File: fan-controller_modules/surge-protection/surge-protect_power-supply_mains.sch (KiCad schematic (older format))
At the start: 10 parts

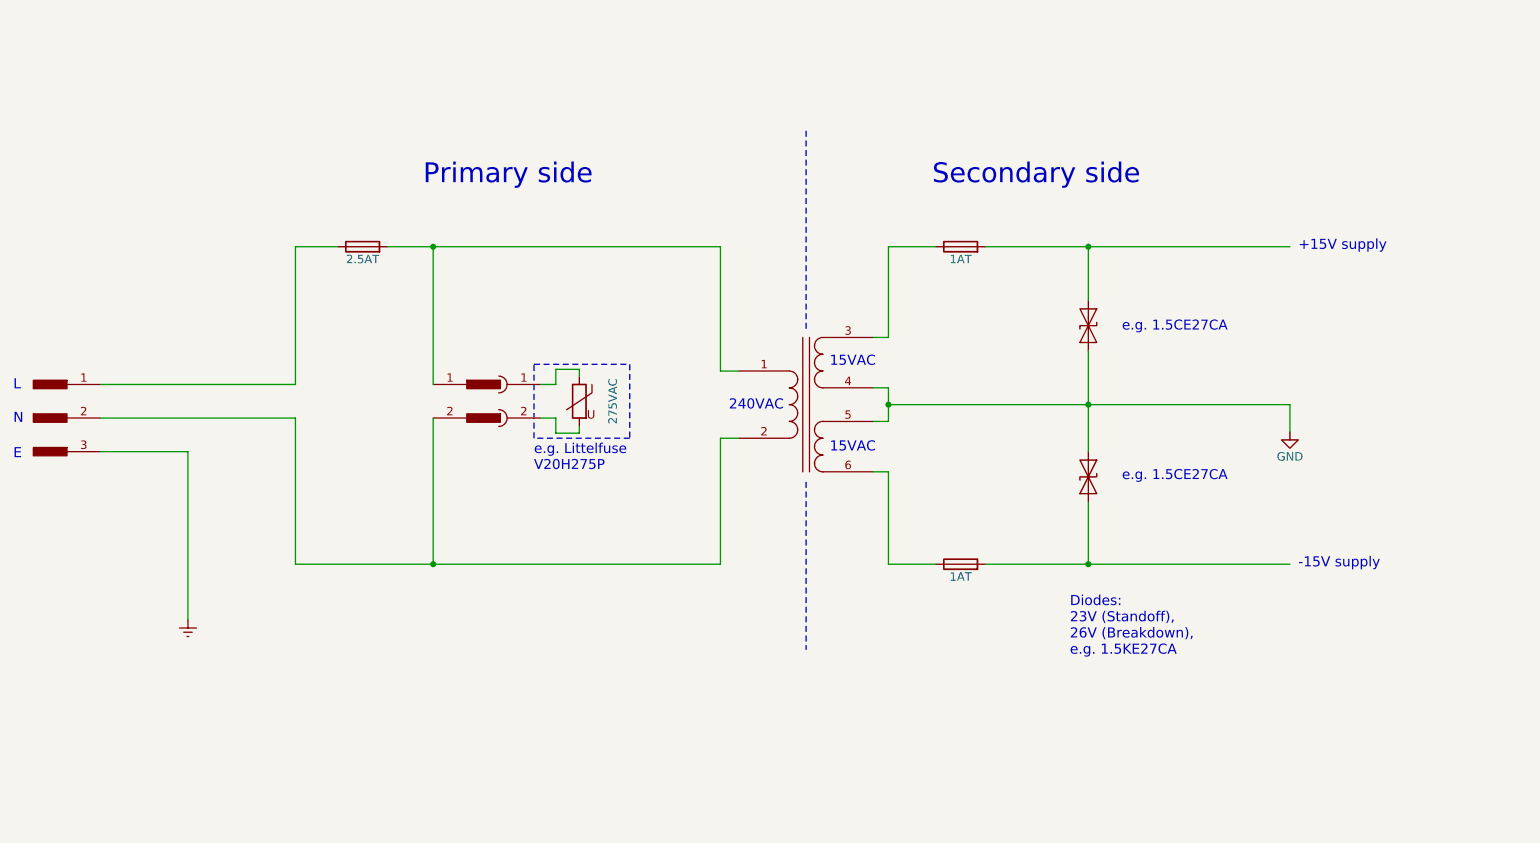
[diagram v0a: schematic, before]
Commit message: Modifying surge protection.
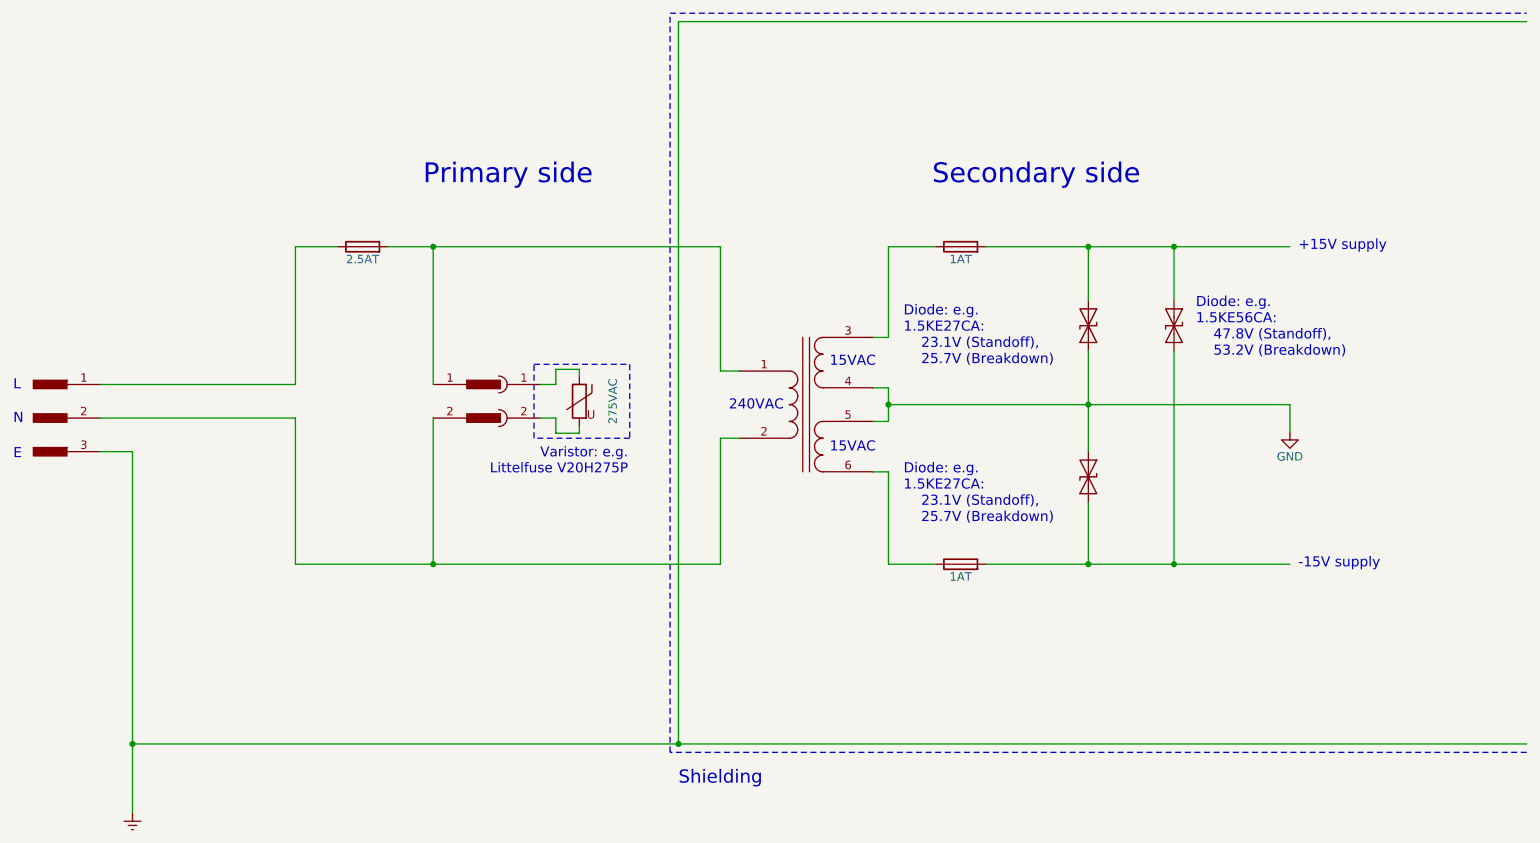
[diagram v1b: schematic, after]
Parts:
- added D?: <=23V, symbol D_TVS
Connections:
- wire segments 39 -> 44
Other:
- note added: "Diode: e.g. \n1.5KE27CA:\n 23.1V (Standoff),\n 25.7V (Breakdown)"
- note added: "Diode: e.g. \n1.5KE56CA:\n 47.8V (Standoff),\n 53.2V (Breakdown)"
- note added: "Shielding"
- note added: "Varistor: e.g. \nLittelfuse V20H275P"
- note removed: "Diodes: \n23V (Standoff),\n26V (Breakdown),\ne.g. 1.5KE27CA"
- note removed: "e.g. 1.5CE27CA"
- note removed: "e.g. Littelfuse\nV20H275P"
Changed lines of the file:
@@
 encoding utf-8
 Sheet 3 4
-Title "Surge protection, Mains power"
+Title "Surge protection, mains power"
 Date "2017-08-15"
 Rev "1.0"
@@
 L Earth #PWR?
 U 1 1 5995D355
-P 2730 5210
-F 0 "#PWR?" H 2730 4960 50  0001 C CNN
-F 1 "Earth" H 2730 5060 50  0001 C CNN
-F 2 "" H 2730 5210 50  0001 C CNN
-F 3 "" H 2730 5210 50  0001 C CNN
-	1    2730 5210
-	1    0    0    -1
-$EndComp
-Text Notes 4790 4330 0    59   ~ 0
-e.g. Littelfuse\nV20H275P
+P 2400 6360
+F 0 "#PWR?" H 2400 6110 50  0001 C CNN
+F 1 "Earth" H 2400 6210 50  0001 C CNN
+F 2 "" H 2400 6360 50  0001 C CNN
+F 3 "" H 2400 6360 50  0001 C CNN
+	1    2400 6360
+	1    0    0    -1
+$EndComp
+Text Notes 5350 4350 2    59   ~ 0
+Varistor: e.g. \nLittelfuse V20H275P
 Text Notes 1690 3850 0    60   ~ 0
 L
@@
 15VAC
 Wire Wire Line
-	2210 4210 2730 4210
-Wire Wire Line
-	2730 4210 2730 5210
+	2210 4210 2400 4210
+Wire Wire Line
+	2400 4210 2400 6360
 Wire Notes Line
 	4790 3690 5360 3690
@@
 Wire Wire Line
 	9290 3930 9290 4090
-Text Notes 8290 3500 0    59   ~ 0
-e.g. 1.5CE27CA
-Text Notes 8290 4390 0    59   ~ 0
-e.g. 1.5CE27CA
 Text Notes 9340 3020 0    60   ~ 0
 +15V supply
@@
 Text Notes 7160 2630 0    118  ~ 0
 Secondary side
-Wire Notes Line
-	6410 2300 6410 3480
-Wire Notes Line
-	6410 4390 6410 5390
 $Comp
 L Transformer_1P_2S T?
@@
 	5900 4130 6010 4130
 Connection ~ 6900 3930
-Text Notes 7980 5430 0    60   ~ 0
-Diodes: \n23V (Standoff),\n26V (Breakdown),\ne.g. 1.5KE27CA
+Text Notes 6990 3700 0    60   ~ 0
+Diode: e.g. \n1.5KE27CA:\n    23.1V (Standoff),\n    25.7V (Breakdown)
+$Comp
+L D_TVS D?
+U 1 1 5996A737
+P 8600 3460
+F 0 "D?" H 8600 3560 50  0001 C CNN
+F 1 "<=23V" H 8600 3580 50  0001 C CNN
+F 2 "" H 8600 3460 50  0001 C CNN
+F 3 "" H 8600 3460 50  0001 C CNN
+	1    8600 3460
+	0    -1   1    0
+$EndComp
+Text Notes 8730 3650 0    60   ~ 0
+Diode: e.g. \n1.5KE56CA:\n    47.8V (Standoff),\n    53.2V (Breakdown)
+Wire Wire Line
+	8600 3310 8600 2990
+Connection ~ 8600 2990
+Wire Wire Line
+	8600 3610 8600 4880
+Connection ~ 8600 4880
+Text Notes 6990 4640 0    60   ~ 0
+Diode: e.g. \n1.5KE27CA:\n    23.1V (Standoff),\n    25.7V (Breakdown)
+Wire Notes Line
+	5600 1600 10700 1600
+Wire Notes Line
+	10700 6000 5600 6000
+Wire Notes Line
+	5600 6000 5600 1600
+Wire Wire Line
+	2400 5950 10700 5950
+Wire Wire Line
+	5650 5950 5650 1650
+Wire Wire Line
+	5650 1650 10700 1650
+Connection ~ 2400 5950
+Connection ~ 5650 5950
+Text Notes 5650 6200 0    79   ~ 0
+Shielding
 $EndSCHEMATC
